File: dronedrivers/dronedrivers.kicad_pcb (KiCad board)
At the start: 4 copper layers, 40 x 50 mm, 54 parts, among them J1 MOTOR, J2 BATT, J4 MOTOR, J5 MOTOR, J6 MOTOR, J7 Conn_02x04_Top_Bottom, J9 USB_C_Receptacle_USB2.0_16P, Q1 AO3400A, Q2 AO3401A, Q3 AO3400A, Q4 AO3400A, Q5 AO3400A, SW1 RST, SW2 BOOT, U1 ESP32-S3-WROOM-1, U3 TXB0104D, U4 ICM-20948, U5 AMS1117-1.8, U6 AMS1117-3.3

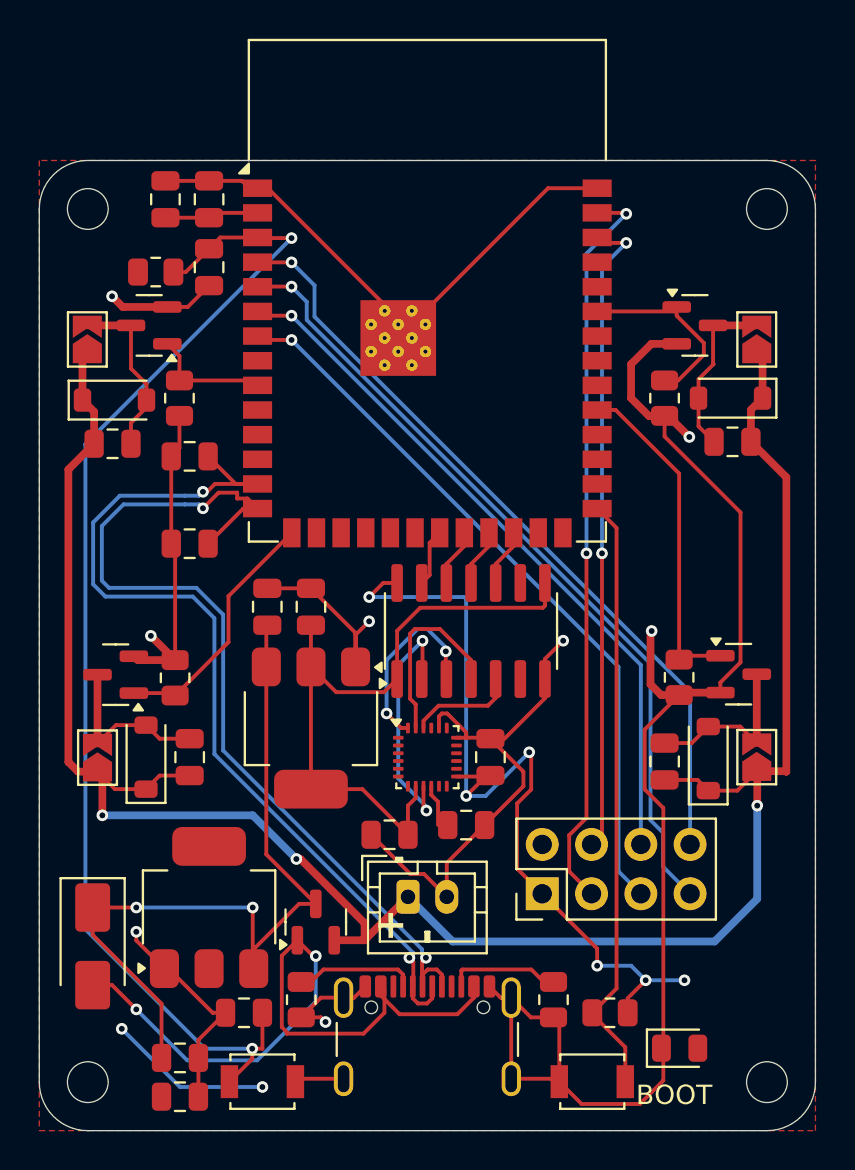
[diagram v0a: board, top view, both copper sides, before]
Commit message: reworked driver pcb
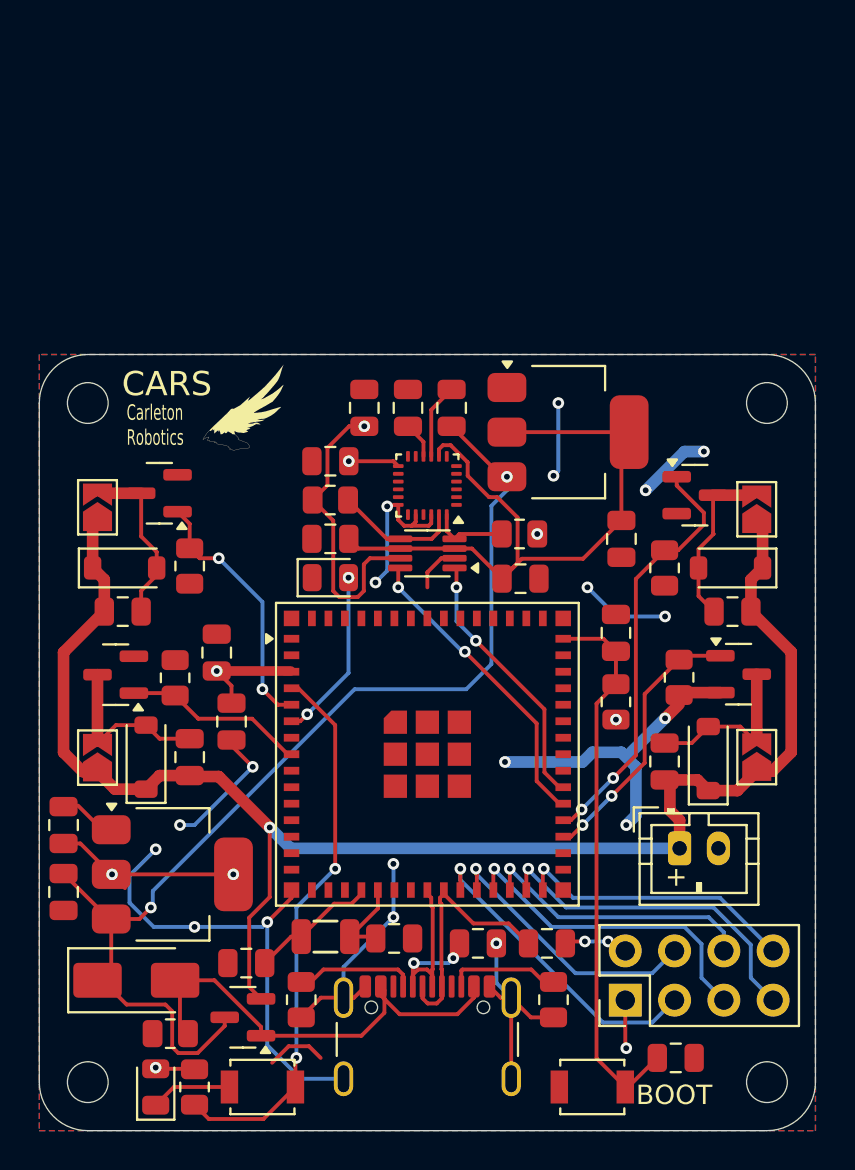
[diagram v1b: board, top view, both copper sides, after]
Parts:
- removed U1: ESP32-S3-WROOM-1, RF_Module:ESP32-S3-WROOM-1
- added C18: 12pF, Capacitor_SMD:C_0805_2012Metric, F.Cu at (143.3, 97.6)
- added C19: 12pF, Capacitor_SMD:C_0805_2012Metric, F.Cu at (135.7, 98.9)
- added C20: 10uF, Capacitor_SMD:C_0805_2012Metric, F.Cu at (141.8, 70.2)
- added C21: 10uF, Capacitor_SMD:C_0805_2012Metric, F.Cu at (140.0, 77.0)
- added D7: LED, LED_SMD:LED_0805_2012Metric, F.Cu at (140.0, 79.0)
- added G***: LOGO, LOGO, F.Cu at (135.5, 70.2)
- added R10: 10K, Resistor_SMD:R_0805_2012Metric, F.Cu at (140.0, 75.0)
- added R11: 100K, Resistor_SMD:R_0805_2012Metric, F.Cu at (131.8, 102.5)
- added R9: 10K, Resistor_SMD:R_0805_2012Metric, F.Cu at (149.8, 76.8)
- added U2: ESP32-S3-MINI-1U, RF_Module:ESP32-S2-MINI-1U, F.Cu at (145.0, 88.1)
- added X1: Q13FC1350000400, PCM_JLCPCB:FC-135R_L3.2-W1.5, F.Cu at (139.8, 97.5)
- C5, C6: value 22uF -> 47pF
- U3: value TXB0104D -> TXB0102DCU; footprint Package_SO:SOIC-14_3.9x8.7mm_P1.27mm -> Package_SO:VSSOP-8_2.3x2mm_P0.5mm
- moved H1 36.4 mm to (162.5, 70.0)
- moved H2 36.4 mm to (127.5, 70.0)
- moved R1 32.5 mm to (154.7, 85.4), turned to 90 degrees
- moved C5 29.2 mm to (147.6, 97.8), turned to 0 degrees
- moved C4 28.2 mm to (154.7, 81.8), turned to 90 degrees
- moved C6 27.6 mm to (151.2, 97.8), turned to 0 degrees
- moved C1 27.1 mm to (134.9, 86.4), turned to -90 degrees
- moved D6 27.1 mm to (131.0, 105.2), turned to 90 degrees
- moved C2 23.4 mm to (134.1, 82.9)
- moved C7 22.4 mm to (157.8, 103.8), turned to 180 degrees
- moved R3 21.8 mm to (133.0, 105.2), turned to -90 degrees
- moved C3 21.7 mm to (144.0, 70.2), turned to 90 degrees
- moved U5 20.2 mm to (152.2, 71.5), turned to 0 degrees
- moved C16 17.3 mm to (140.0, 73.0), turned to 180 degrees
- moved SW1 17.0 mm to (153.5, 105.2), turned to 0 degrees
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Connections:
- J7 pad 5: IO14 -> IO11
- J7 pad 6: IO13 -> IO12
- J7 pad 7: IO12 -> IO13
- J7 pad 8: IO11 -> IO14
- U3 pad 1: +1V8 -> IO5
- U3 pad 2: Net-(U3-A1) -> GND
- U3 pad 3: Net-(U3-A2) -> +1V8
- U3 pad 4: Net-(U3-A3) -> Net-(U3-A2)
- U3 pad 5: Net-(U3-A4) -> Net-(U3-A1)
- U3 pad 6: unconnected-(U3-NC-Pad6) -> +1V8
- U3 pad 7: GND -> +3.3V
- U3 pad 8: +1V8 -> IO6
- U4 pad 22: Net-(U3-A4) -> GND
- U4 pad 23: Net-(U3-A3) -> Net-(U3-A1)
- U4 pad 9: Net-(U3-A1) -> GND
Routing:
- net GND: track 181.4 -> 112.1 mm, vias 8 -> 21
- net D-: track 48.4 -> 11.8 mm
- net D+: track 48.5 -> 13.0 mm, vias 2 -> 0
- net EN: track 62.6 -> 28.7 mm, vias 2 -> 0
- net IO12: track 41.8 -> 14.4 mm
- net +BATT: track 108.9 -> 81.6 mm, vias 3 -> 1
- net IO11: track 40.3 -> 16.8 mm
- net IO14: track 37.8 -> 14.7 mm
- net IO9: track 38.6 -> 16.2 mm, vias 2 -> 1
- net IO10: track 33.4 -> 14.2 mm, vias 2 -> 1
- net IO13: track 36.5 -> 17.6 mm
- net +3.3V: track 57.8 -> 40.0 mm, vias 8 -> 9
- net VIN: track 41.2 -> 57.0 mm
- net Net-(D2-A): track 36.7 -> 23.4 mm, vias 2 -> 0
- net IO6: track 3.07 -> 15.9 mm, vias 0 -> 2
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- added copper zone on B.Cu, net +3.3V
- added copper zone on F.Cu, net GND
- removed copper zone on F.Cu, net +3.3V
- removed copper zone on In1.Cu, net GND
- removed copper zone on In2.Cu, net GND
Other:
- board size 40 x 50 mm -> 40 x 40 mm
- copper layers 4 -> 2
- board text added: "1,4,37,38 40,39 21,26 47,33,34,48"
- board text added: "CARS"
- board text added: "Carleton Robotics"
